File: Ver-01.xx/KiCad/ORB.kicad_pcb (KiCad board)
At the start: 2 copper layers, 104 x 72 mm, 141 parts, among them IC1 LM3940-3.3, IC2 LM340-5.0, IC3 LM340-5.0, IC4 TB6612FNG, IC5 TB6612FNG, J1 LOETJUMPER, J2 USB_C_Receptacle_USB2.0, J3 Conn_02x03_Odd_Even, K10 NXT-Socket, K11 NXT-Socket, K12 Wannenstecker, K13 Wannenstecker, K14 NXT-Socket, K15 Stiftleiste_1x06, K16 NXT-Socket, K17 Wannenstecker, K18 Wannenstecker, K19 NXT-Socket, K2 Anschlussklemme, K20 NXT-Socket, K21 Wannenstecker, K24 Stiftleiste_2x02, K25 Stiftleiste_1x04, K26 Stiftleiste_1x02_G_2,54, K4 Wannenstecker, K6 NXT-Socket, K7 NXT-Socket, K8 Wannenstecker, K9 Wannenstecker, U1 RN4678, X1 STM32F405VGT, Y1 Crystal

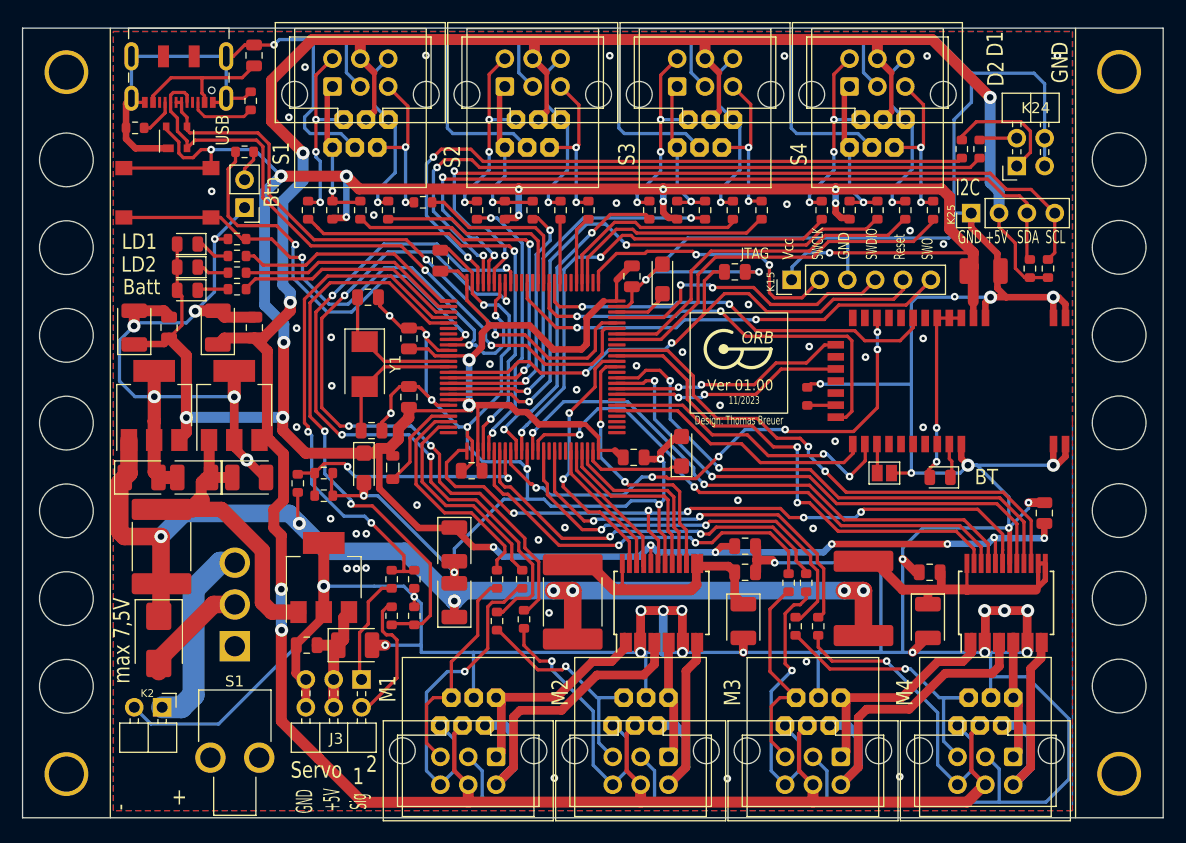
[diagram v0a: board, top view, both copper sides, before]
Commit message: USB connector changed
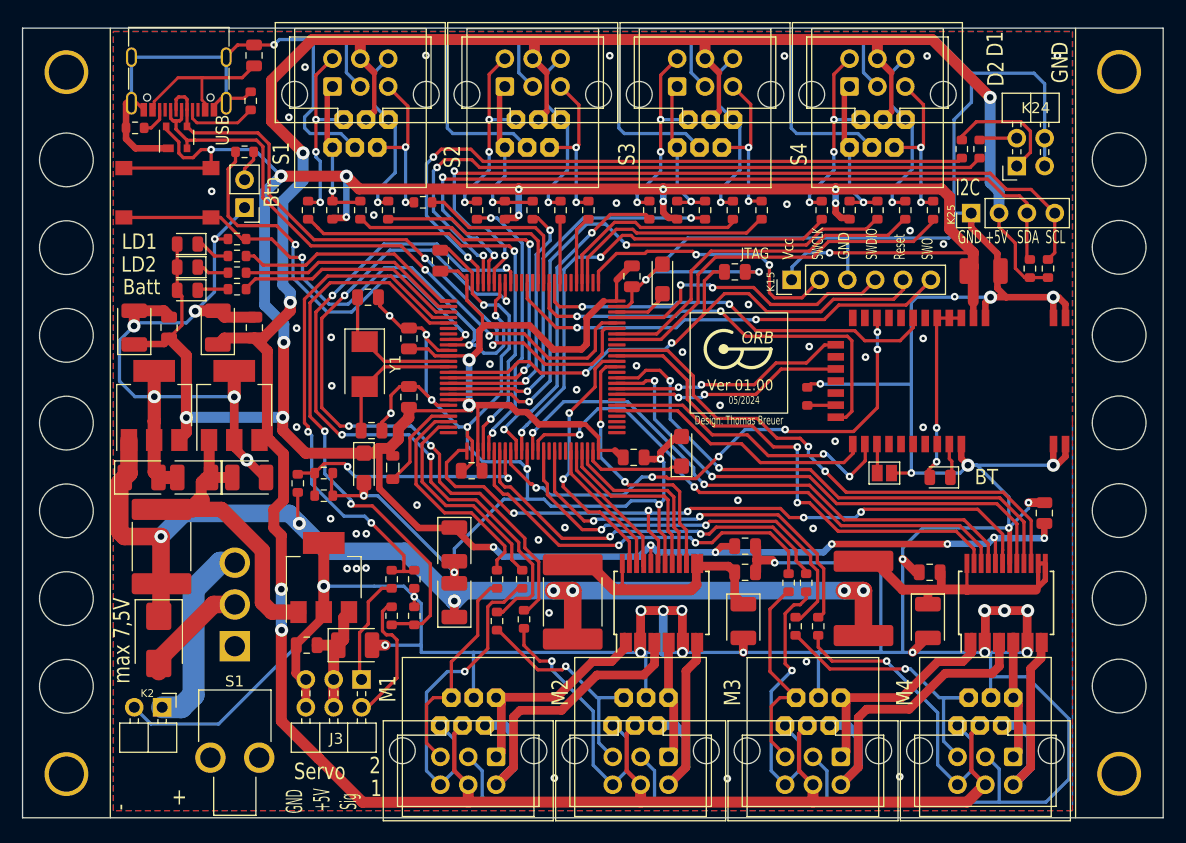
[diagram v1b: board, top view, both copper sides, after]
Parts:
- J2: footprint Connector_USB:USB_C_Receptacle_JAE_DX07S016JA1R1500 -> Connector_USB:USB_C_Receptacle_G-Switch_GT-USB-7010ASV
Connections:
- FILTER1 pad 2: USBDM -> USBDP
- FILTER1 pad 3: USBDP -> USBDM
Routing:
- net USBDP: track 56.5 -> 58.6 mm
- net USBDM: track 61.6 -> 59.7 mm
- net Net-(C7-Pad2): track 13.3 -> 14.3 mm
- net Net-(J2-CC2): track 3.44 -> 2.60 mm
- net Net-(J2-CC1): track 6.01 -> 6.75 mm
